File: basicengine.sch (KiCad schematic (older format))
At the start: 109 parts, among them J1 MicroSD Card, J10 Conn_01x01, J12 Conn_02x20_Counter_Clockwise, J17 PSX CONTROLLER, J2 USB KBD Alt, J3 Conn_01x06, J4 Conn_01x03, J5 VIDEO, J6 USB KBD, J7 AUDIO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

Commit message: sch: replace THT electrolytics with ceramic SMT caps
Reduces regulator in/out capacitors from 220u to 22u; tested by writing
data from network to SD card, seems to be stable.
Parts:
- C11, C12: value 220u -> 22u; footprint Capacitors_Elko_ThroughHole:Elko_vert_11x5mm_RM2.5_CopperClear -> Capacitors_SMD:C_1206_HandSoldering; symbol CP -> C
- C9: footprint Capacitors_Elko_ThroughHole:Elko_vert_11x5mm_RM2.5_CopperClear -> Capacitors_SMD:C_1206_HandSoldering; symbol CP -> C
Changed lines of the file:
@@
 EESchema Schematic File Version 2
-LIBS:basicengine-rescue
 LIBS:power
-LIBS:device
-LIBS:switches
-LIBS:relays
-LIBS:motors
-LIBS:transistors
-LIBS:conn
-LIBS:linear
-LIBS:regul
-LIBS:74xx
-LIBS:cmos4000
-LIBS:adc-dac
-LIBS:memory
-LIBS:xilinx
-LIBS:microcontrollers
-LIBS:dsp
-LIBS:microchip
-LIBS:analog_switches
-LIBS:motorola
-LIBS:texas
-LIBS:intel
-LIBS:audio
-LIBS:interface
-LIBS:digital-audio
-LIBS:philips
-LIBS:display
-LIBS:cypress
-LIBS:siliconi
-LIBS:opto
-LIBS:atmel
-LIBS:contrib
-LIBS:valves
-LIBS:ESP8266
-LIBS:NXP
-LIBS:nxp
-LIBS:VS23S010
-LIBS:ab2_7segment
-LIBS:ab2_audio
-LIBS:ab2_usb
-LIBS:reg33
-LIBS:psx
 LIBS:basicengine-cache
 EELAYER 25 0
@@
 GND
 $Comp
-L CP C9
+L C C9
 U 1 1 59C65936
 P 7300 3450
 F 0 "C9" H 7325 3550 50  0000 L CNN
 F 1 "10u" H 7325 3350 50  0000 L CNN
-F 2 "Capacitors_Elko_ThroughHole:Elko_vert_11x5mm_RM2.5_CopperClear" H 7338 3300 50  0001 C CNN
+F 2 "Capacitors_SMD:C_1206_HandSoldering" H 7338 3300 50  0001 C CNN
 F 3 "" H 7300 3450 50  0001 C CNN
 	1    7300 3450
@@
 	4650 5500 5650 5500
 $Comp
-L CP C11
+L C C11
 U 1 1 59C68B94
 P 9900 5650
 F 0 "C11" H 9925 5750 50  0000 L CNN
-F 1 "220u" H 9925 5550 50  0000 L CNN
-F 2 "Capacitors_Elko_ThroughHole:Elko_vert_11x5mm_RM2.5_CopperClear" H 9938 5500 50  0001 C CNN
+F 1 "22u" H 9925 5550 50  0000 L CNN
+F 2 "Capacitors_SMD:C_1206_HandSoldering" H 9938 5500 50  0001 C CNN
 F 3 "" H 9900 5650 50  0001 C CNN
 	1    9900 5650
@@
 $EndComp
 $Comp
-L CP C12
+L C C12
 U 1 1 59C68C0B
 P 10700 5650
 F 0 "C12" H 10725 5750 50  0000 L CNN
-F 1 "220u" H 10725 5550 50  0000 L CNN
-F 2 "Capacitors_Elko_ThroughHole:Elko_vert_11x5mm_RM2.5_CopperClear" H 10738 5500 50  0001 C CNN
+F 1 "22u" H 10725 5550 50  0000 L CNN
+F 2 "Capacitors_SMD:C_1206_HandSoldering" H 10738 5500 50  0001 C CNN
 F 3 "" H 10700 5650 50  0001 C CNN
 	1    10700 5650

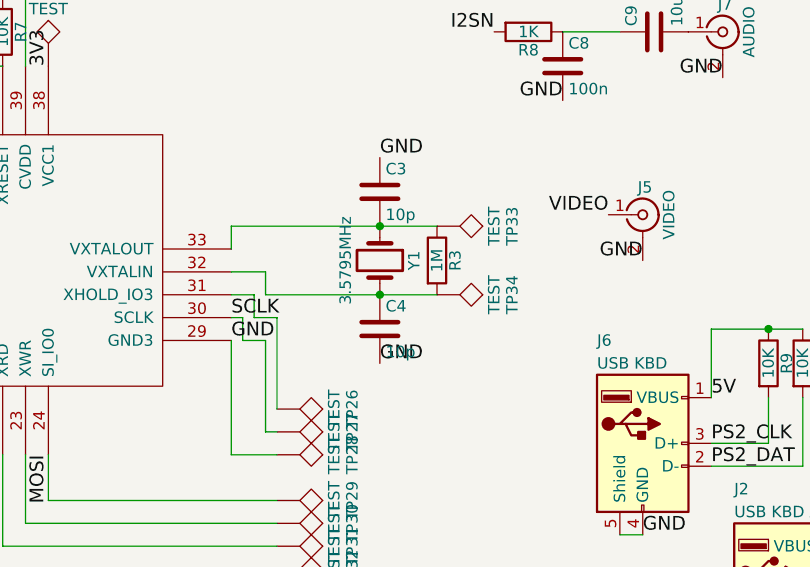
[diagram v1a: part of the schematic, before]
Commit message: sch: change VS23S010 oscillator caps from 10p to 56p
Yields more accurate color burst frequency, fixes B/W display on Sony
KX-14CP1.
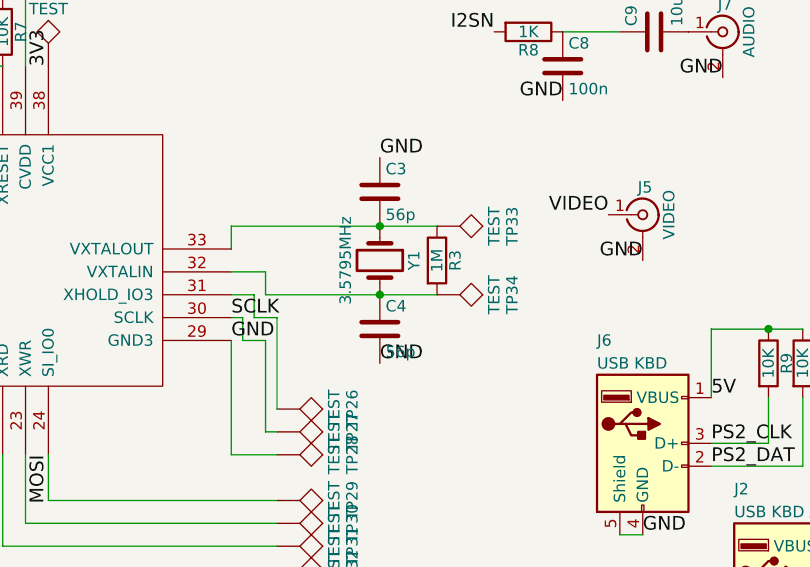
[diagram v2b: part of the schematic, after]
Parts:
- C3, C4: value 10p -> 56p
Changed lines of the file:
@@
 P 6100 4150
 F 0 "C3" H 6125 4250 50  0000 L CNN
-F 1 "10p" H 6125 4050 50  0000 L CNN
+F 1 "56p" H 6125 4050 50  0000 L CNN
 F 2 "Capacitors_SMD:C_1206_HandSoldering" H 6138 4000 50  0001 C CNN
 F 3 "" H 6100 4150 50  0001 C CNN
@@
 P 6100 4750
 F 0 "C4" H 6125 4850 50  0000 L CNN
-F 1 "10p" H 6125 4650 50  0000 L CNN
+F 1 "56p" H 6125 4650 50  0000 L CNN
 F 2 "Capacitors_SMD:C_1206_HandSoldering" H 6138 4600 50  0001 C CNN
 F 3 "" H 6100 4750 50  0001 C CNN
